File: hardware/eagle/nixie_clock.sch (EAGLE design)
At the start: 81 parts, among them IC1 74141N, IC10 7477N, IC11 74141N, IC12 7477N, IC13 74HCT259N, IC15 7477N, IC2 7477N, IC3 74141N, IC4 7477N, IC5 74141N, IC6 7477N, IC7 74141N, IC8 7477N, IC9 74141N, J1 RASPBERRYPI-40-PIN-GPIO, J1_180V 22-27-2021-02, J1_5V1 22-27-2021-02, J1_5V2 22-27-2021-02, K1 4052, SW1 ROTARTY_ENCODER

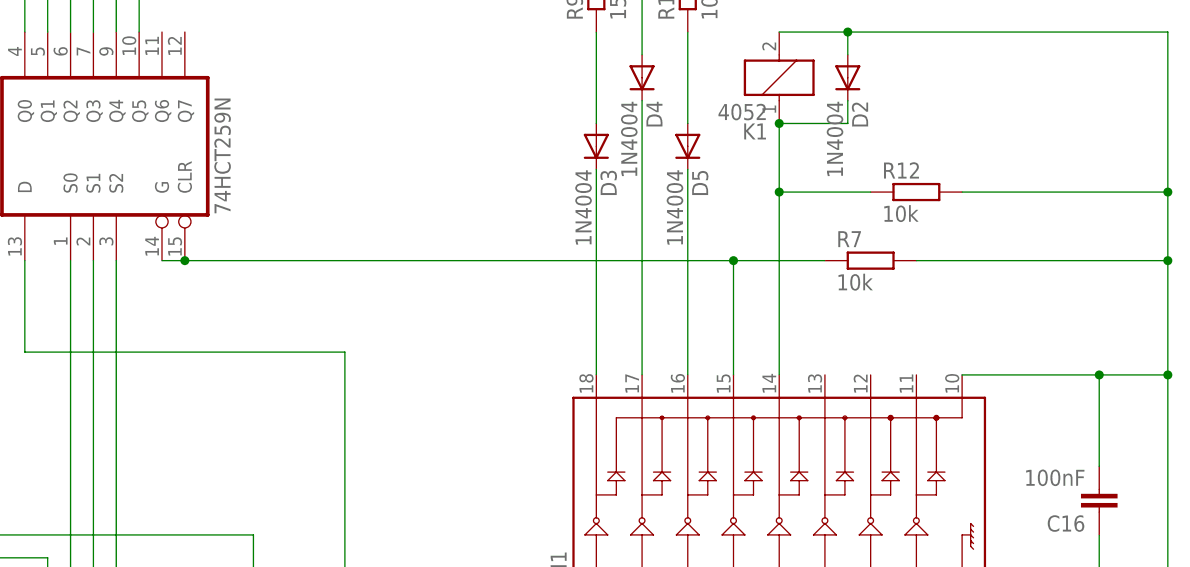
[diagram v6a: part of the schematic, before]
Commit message: Fixed bug related to multiplexed data
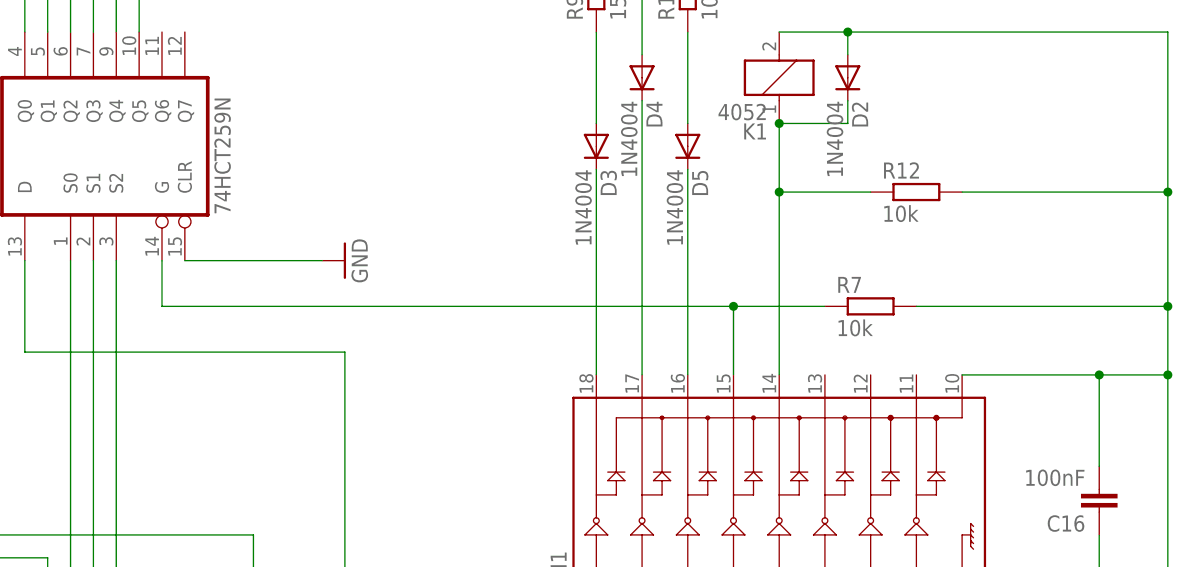
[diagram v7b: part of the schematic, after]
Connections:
- net GND: now also IC13A.CLR
- net N$140: no longer IC13A.CLR
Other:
- moved on the sheet: R7
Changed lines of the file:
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@@
 <part name="R11" library="rcl" deviceset="R-EU_" device="0204/7" value="100"/>
 <part name="R12" library="rcl" deviceset="R-EU_" device="0204/7" value="10k"/>
+<part name="GND4" library="supply1" deviceset="GND" device=""/>
 </parts>
 <sheets>
@@
 <attribute name="MPN" x="469.9" y="15.24" size="1.778" layer="96" display="off"/>
 </instance>
-<instance part="R7" gate="G$1" x="515.62" y="200.66"/>
+<instance part="R7" gate="G$1" x="515.62" y="195.58"/>
 <instance part="GND1" gate="1" x="350.52" y="60.96"/>
 <instance part="C18" gate="G$1" x="340.36" y="76.2"/>
@@
 <instance part="R11" gate="G$1" x="495.3" y="231.14" rot="R90"/>
 <instance part="R12" gate="G$1" x="520.7" y="208.28"/>
+<instance part="GND4" gate="1" x="457.2" y="200.66" rot="R90"/>
 </instances>
 <busses>
@@
 <junction x="350.52" y="66.04"/>
 </segment>
+<segment>
+<pinref part="IC13" gate="A" pin="CLR"/>
+<wire x1="439.42" y1="200.66" x2="454.66" y2="200.66" width="0.1524" layer="91"/>
+<pinref part="GND4" gate="1" pin="GND"/>
+</segment>
 </net>
 <net name="N$104" class="0">
@@
 <net name="N$140" class="0">
 <segment>
+<pinref part="ULN1" gate="G$1" pin="15"/>
+<pinref part="R7" gate="G$1" pin="1"/>
+<wire x1="500.38" y1="195.58" x2="500.38" y2="187.96" width="0.1524" layer="91"/>
+<wire x1="500.38" y1="195.58" x2="510.54" y2="195.58" width="0.1524" layer="91"/>
 <pinref part="IC13" gate="A" pin="G"/>
-<pinref part="IC13" gate="A" pin="CLR"/>
-<wire x1="436.88" y1="200.66" x2="439.42" y2="200.66" width="0.1524" layer="91"/>
-<pinref part="ULN1" gate="G$1" pin="15"/>
-<wire x1="439.42" y1="200.66" x2="500.38" y2="200.66" width="0.1524" layer="91"/>
-<wire x1="500.38" y1="200.66" x2="500.38" y2="187.96" width="0.1524" layer="91"/>
-<junction x="439.42" y="200.66"/>
-<pinref part="R7" gate="G$1" pin="1"/>
-<wire x1="500.38" y1="200.66" x2="510.54" y2="200.66" width="0.1524" layer="91"/>
-<junction x="500.38" y="200.66"/>
+<wire x1="436.88" y1="200.66" x2="436.88" y2="195.58" width="0.1524" layer="91"/>
+<wire x1="436.88" y1="195.58" x2="500.38" y2="195.58" width="0.1524" layer="91"/>
+<junction x="500.38" y="195.58"/>
 </segment>
 </net>
@@
 <junction x="477.52" y="22.86"/>
 <pinref part="R7" gate="G$1" pin="2"/>
-<wire x1="520.7" y1="200.66" x2="548.64" y2="200.66" width="0.1524" layer="91"/>
-<wire x1="548.64" y1="200.66" x2="548.64" y2="187.96" width="0.1524" layer="91"/>
+<wire x1="520.7" y1="195.58" x2="548.64" y2="195.58" width="0.1524" layer="91"/>
+<wire x1="548.64" y1="195.58" x2="548.64" y2="187.96" width="0.1524" layer="91"/>
 <junction x="548.64" y="187.96"/>
 <pinref part="SV16" gate="G$1" pin="1"/>
@@
 <pinref part="R12" gate="G$1" pin="2"/>
 <wire x1="525.78" y1="208.28" x2="548.64" y2="208.28" width="0.1524" layer="91"/>
-<wire x1="548.64" y1="208.28" x2="548.64" y2="200.66" width="0.1524" layer="91"/>
-<junction x="548.64" y="200.66"/>
+<wire x1="548.64" y1="208.28" x2="548.64" y2="195.58" width="0.1524" layer="91"/>
+<junction x="548.64" y="195.58"/>
 <wire x1="513.08" y1="226.06" x2="548.64" y2="226.06" width="0.1524" layer="91"/>
 <wire x1="548.64" y1="226.06" x2="548.64" y2="208.28" width="0.1524" layer="91"/>

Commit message: Updated eagle project
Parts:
- removed SV1, SV11, SV13, SV3, SV5, SV7, SV9: (no value), con-lstb:MA06-1
- added J10, J4, J5, J6, J7, J8, J9: (no value), SparkFun-Connectors:M08
- added J2: (no value), SparkFun-Connectors:M05X2PTH
- added J3: (no value), SparkFun-Connectors:M04PTH
- added SV17: (no value), con-lstb:MA09-2
- SV10, SV12, SV14, SV2, SV4, SV6, SV8: device con-lstb:MA05-1 -> SparkFun-Connectors:M07
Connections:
- new net BLUE: J3.3, R11.2, SV10.7, SV12.7, SV2.7, SV4.7, SV6.7, SV8.7
- new net GREEN: J3.2, R10.2, SV10.6, SV12.6, SV2.6, SV4.6, SV6.6, SV8.6
- new net GROUND: C1.2, C10.2, C11.2, C12.2, C13.2, C16.2, C17.2, C2.2, C3.2, C4.2, C5.2, C6.2, C7.2, C8.2, C9.2, D2.A, IC10P.VCC, IC11P.VCC, IC12P.VCC, IC13A.D, IC13P.VCC, IC15P.VCC, IC1P.VCC, IC2P.VCC, IC3P.VCC, IC4P.VCC, IC5P.VCC, IC6P.VCC, IC7P.VCC, IC8P.VCC, IC9P.VCC, J1_5V1-2.S, J3.4, K11.2, R12.2, R7.2, R8.1, SV10.5, SV12.5, SV16.1, SV2.5, SV4.5, SV6.5, SV8.5, ULN1.10
- new net N$145: J1.3.3V@1, J2.1, SV17.1
- new net N$150: J7.8, R4.1
- new net N$153: J1.5V@4, J2.4, SV17.4
- new net N$154: J1.SDA, J2.3, SV17.3
- new net N$155: J1.SCL, J2.5, SV17.5
- new net N$156: J1.GND@6, J2.6, J2.9, SV17.6
- new net N$157: J1.ID_SD, SV17.7
- new net N$158: J1.ID_SC, SV17.9
- new net N$159: J1.TXO, SV17.8
- new net N$160: J1.RXI, SV17.10
- new net N$161: J1.MOSI, SV17.11
- new net N$162: J1.MISO, SV17.13
- new net N$163: J1.SCLK, SV17.15
- new net N$164: J4.8, R1.1
- new net N$165: J1.GND@9, SV17.12
- new net N$166: J1.CE0, SV17.14
- new net N$167: J1.CE1, SV17.16
- new net N$168: J1.GND@14, SV17.18
- new net N$169: J6.8, R3.1
- new net N$170: R1.2, R2.2, R3.2, R4.2, R5.2, R6.2
- new net N$171: J5.8, R2.1
- new net N$172: J1.5V@2, J2.2, SV17.2
- new net RED: J3.1, R9.2, SV10.4, SV12.4, SV2.4, SV4.4, SV6.4, SV8.4
- net N$1: now also IN-8-1.4, J10.1; no longer R2.1, SV4.3
- net N$10: now also IN-8-1.9, J10.6; no longer IC1A.9, SV2.5
- net N$100: now also IC9A.0, J8.7; no longer IC11A.5, SV11.3
- net N$101: now also IC9A.3, SV10.1; no longer IC11A.6, SV11.4
- net N$102: now also IC9A.2, SV10.2; no longer IC11A.7, SV11.5
- net N$103: now also IC9A.1, SV10.3; no longer IC11A.8, SV11.6
- net N$104: now also J10.8; no longer SV14.3
- net N$105: now also IC11A.6, J9.3; no longer IN-8-1.1, SV14.2
- net N$106: now also IC11A.7, J9.4; no longer IN-8-1.2, SV14.1
- net N$107: now also IC11A.8, J9.5; no longer IN-8-1.0, SV14.4
- net N$109: now also IC11A.9, J9.6; no longer IN-8-1.9, SV14.5
- net N$11: now also IN-8-1.0, J10.7; no longer IC1A.3, SV1.1
- net N$110: now also IC11A.0, J9.7; no longer IN-8-1.8, SV13.6
- net N$111: now also IC11A.3, SV12.1; no longer IN-8-1.7, SV13.5
- net N$112: now also IC11A.2, SV12.2; no longer IN-8-1.6, SV13.4
- net N$113: now also IC11A.1, SV12.3; no longer IN-8-1.5, SV13.3
- net N$114: now also J8.8, R5.1; no longer IN-8-1.4, SV13.2
- net N$115: now also J9.8, R6.1; no longer IN-8-1.3, SV13.1
- net N$12: now also IN-8-1.3, SV14.1; no longer IC1A.4, SV1.2
- net N$13: now also IN-8-1.2, SV14.2; no longer IC1A.5, SV1.3
- net N$14: now also IN-8-1.1, SV14.3; no longer IC1A.6, SV1.4
- net N$15: now also D1.RED_CATHODE, SV14.4; no longer IC1A.7, SV1.5
- net N$152: now also J1.3.3V@17, SV17.17; no longer C1.2, C10.2, C11.2, C12.2, C13.2, C16.2, C17.2, C2.2, C3.2, C4.2, C5.2, C6.2, C7.2, C8.2, C9.2, D2.A, IC10P.VCC, IC11P.VCC, IC12P.VCC, IC13A.D, IC13P.VCC, IC15P.VCC, IC1P.VCC, IC2P.VCC, IC3P.VCC, IC4P.VCC, IC5P.VCC, IC6P.VCC, IC7P.VCC, IC8P.VCC, IC9P.VCC, J1_5V1-2.S, K11.2, R12.2, R7.2, R8.1, SV16.1, ULN1.10
- net N$18: now also IC1A.4, J4.1; no longer IC3A.2, SV4.1
- net N$19: now also IC1A.5, J4.2; no longer IC3A.1, SV4.2
- net N$20: now also D1.BLUE_CATHODE, SV14.7; no longer IC3A.0, SV4.4
- net N$21: now also D1.ANODE, SV14.5; no longer IC3A.9, SV4.5
- net N$22: now also D1.GREEN_CATHODE, SV14.6; no longer IC3A.3, SV3.1
- net N$23: now also IC1A.6, J4.3; no longer IC3A.4, SV3.2
- net N$24: now also IC1A.7, J4.4; no longer IC3A.5, SV3.3
- net N$25: now also IC1A.8, J4.5; no longer IC3A.6, SV3.4
- net N$26: now also IC1A.9, J4.6; no longer IC3A.7, SV3.5
- net N$27: now also IC1A.3, SV2.1; no longer IC3A.8, SV3.6
- net N$28: now also IC1A.2, SV2.2; no longer R3.1, SV6.3
- net N$34: now also IC1A.1, SV2.3; no longer IC5A.2, SV6.1
- net N$35: now also IC1A.0, J4.7; no longer IC5A.1, SV6.2
- net N$36: now also IC3A.4, J5.1; no longer IC5A.0, SV6.4
- net N$37: now also IC3A.5, J5.2; no longer IC5A.9, SV6.5
- net N$38: now also IC3A.6, J5.3; no longer IC5A.3, SV5.1
- net N$39: now also IC3A.7, J5.4; no longer IC5A.4, SV5.2
- net N$40: now also IC3A.8, J5.5; no longer IC5A.5, SV5.3
- net N$41: now also IC3A.9, J5.6; no longer IC5A.6, SV5.4
- net N$42: now also IC3A.0, J5.7; no longer IC5A.7, SV5.5
- net N$43: now also IC3A.3, SV4.1; no longer IC5A.8, SV5.6
- net N$49: now also IC3A.2, SV4.2; no longer R4.1, SV8.3
- net N$50: now also IC3A.1, SV4.3; no longer IC7A.2, SV8.1
- net N$51: now also IC5A.4, J6.1; no longer IC7A.1, SV8.2
- net N$52: now also IC5A.5, J6.2; no longer IC7A.0, SV8.4
- net N$53: now also IC5A.6, J6.3; no longer IC7A.9, SV8.5
- net N$54: now also IC5A.7, J6.4; no longer IC7A.3, SV7.1
- net N$55: now also IC5A.8, J6.5; no longer IC7A.4, SV7.2
- net N$56: now also IC5A.9, J6.6; no longer IC7A.5, SV7.3
- net N$57: now also IC5A.0, J6.7; no longer IC7A.6, SV7.4
- net N$58: now also IC5A.3, SV6.1; no longer IC7A.7, SV7.5
- net N$6: now also IN-8-1.5, J10.2; no longer R1.1, SV2.3
- net N$64: now also IC5A.2, SV6.2; no longer IC7A.8, SV7.6
- net N$65: now also IC5A.1, SV6.3; no longer R5.1, SV10.3
- net N$66: now also IC7A.4, J7.1; no longer IC9A.2, SV10.1
- net N$67: now also IC7A.5, J7.2; no longer IC9A.1, SV10.2
- net N$68: now also IC7A.6, J7.3; no longer IC9A.0, SV10.4
- net N$69: now also IC7A.7, J7.4; no longer IC9A.9, SV10.5
- net N$7: now also IN-8-1.6, J10.3; no longer IC1A.1, SV2.2
- net N$70: now also IC7A.8, J7.5; no longer IC9A.3, SV9.1
- net N$71: now also IC7A.9, J7.6; no longer IC9A.4, SV9.2
- net N$72: now also IC7A.0, J7.7; no longer IC9A.5, SV9.3
- net N$73: now also IC7A.3, SV8.1; no longer IC1A.8, SV1.6
- net N$79: now also IC7A.2, SV8.2; no longer IC9A.6, SV9.4
- net N$8: now also IN-8-1.7, J10.4; no longer IC1A.2, SV2.1
- net N$80: now also IC7A.1, SV8.3; no longer IC9A.7, SV9.5
- net N$81: now also IC9A.4, J8.1; no longer IC9A.8, SV9.6
- net N$82: now also IC9A.5, J8.2; no longer R6.1, SV12.3
- net N$83: now also IC9A.6, J8.3; no longer IC11A.2, SV12.1
- net N$84: now also IC9A.7, J8.4; no longer IC11A.1, SV12.2
- net N$85: now also IC9A.8, J8.5; no longer IC11A.0, SV12.4
- net N$86: now also IC9A.9, J8.6; no longer IC11A.9, SV12.5
- net N$87: now also IC11A.4, J9.1; no longer IC11A.3, SV11.1
- net N$88: now also IC11A.5, J9.2; no longer IC11A.4, SV11.2
- net N$9: now also IN-8-1.8, J10.5; no longer IC1A.0, SV2.4
- net VCC: no longer R1.2, R2.2, R3.2, R4.2, R5.2, R6.2
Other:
- note added: "GND"
- note added: "SIA"
- note added: "SIB"
- note added: "SW"
- note added: "VCC"
- moved on the sheet: C18, D1, IN-8-1, J1_180V-1, J1_180V-2, K1, R1, R2, R3, R4, R5, R6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
